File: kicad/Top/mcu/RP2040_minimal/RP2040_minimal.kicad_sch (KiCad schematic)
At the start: 39 parts, among them J2 Conn_01x02, U2 W25Q128JVS, U3 RP2040, Y1 ABLS-12.000MHZ-B4-T

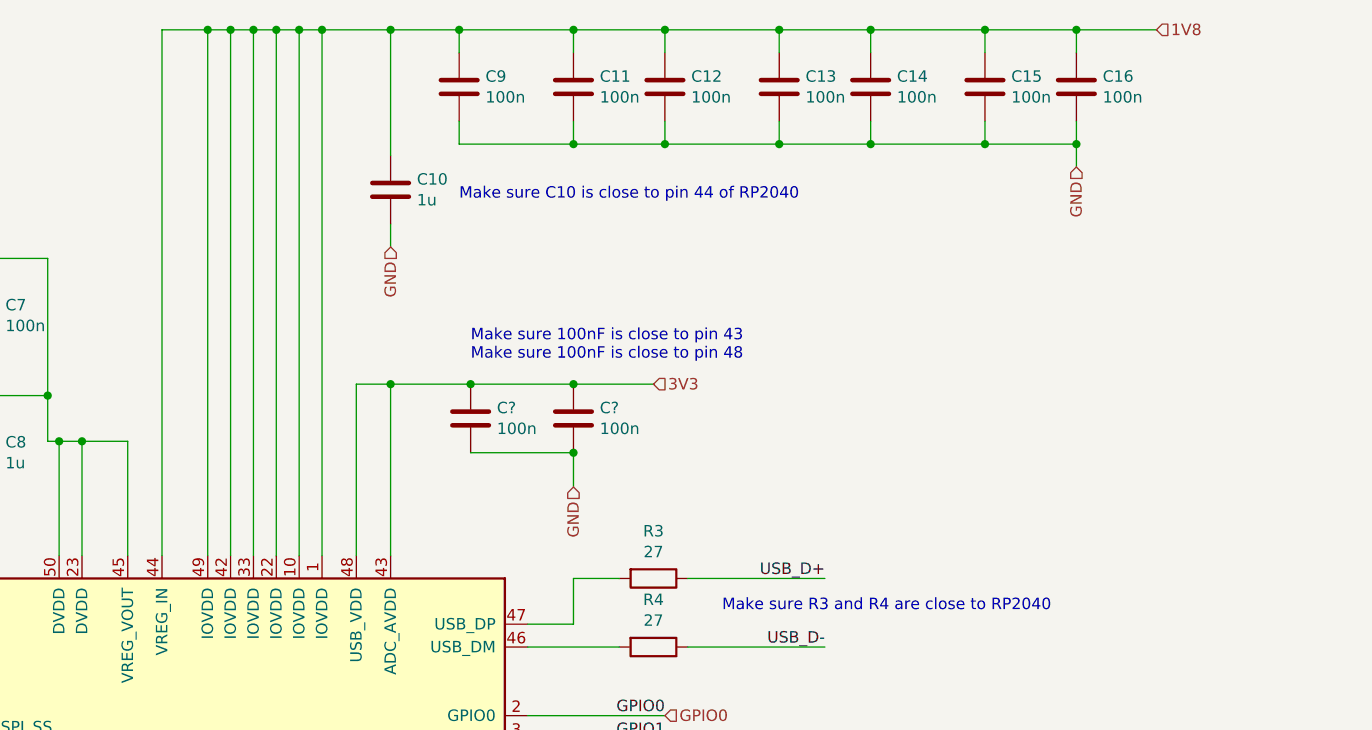
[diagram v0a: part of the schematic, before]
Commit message: Revert "Seperated and added 3V3 to MCU for USB and AVD supply"
This reverts commit dff833df8ca7cc74c4733d65dcaa8f38f7d04b29.
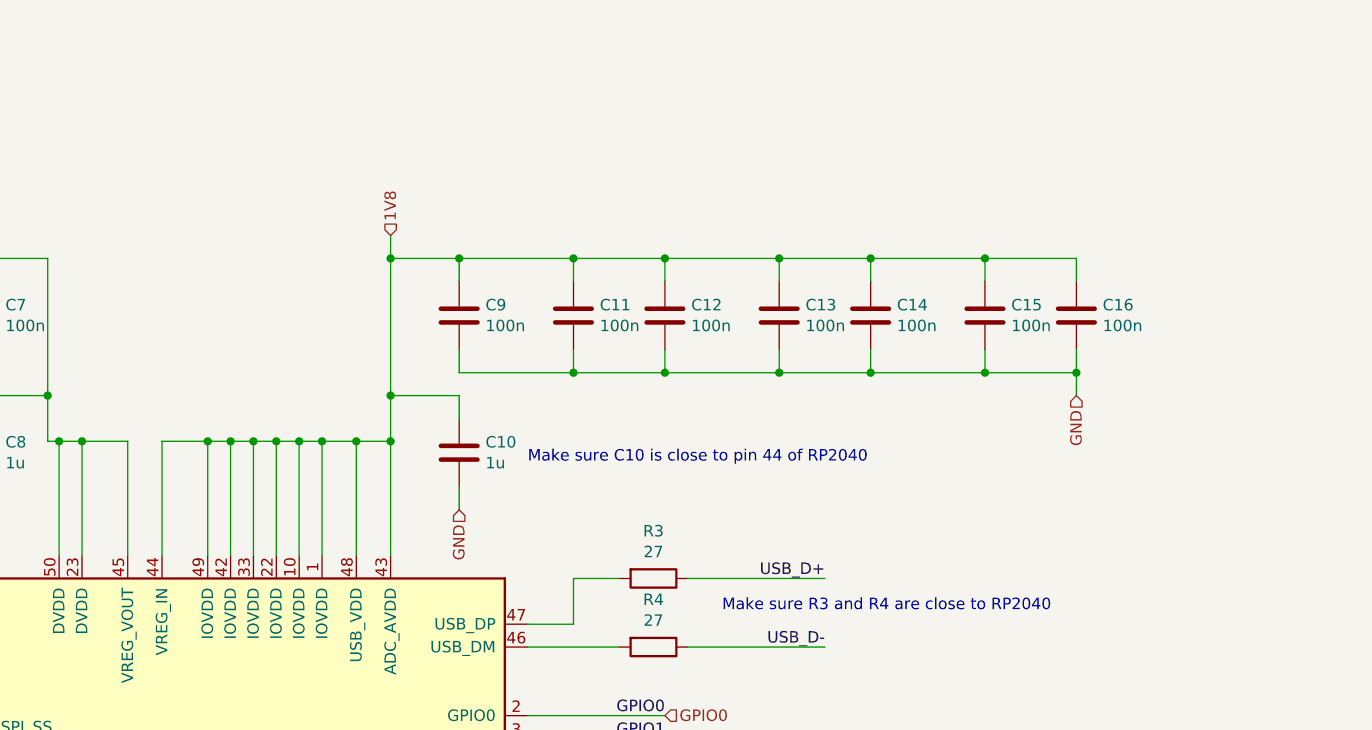
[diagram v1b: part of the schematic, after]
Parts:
- removed C? (x2): 100n, Capacitor_SMD:C_0402_1005Metric, symbol Device:C
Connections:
- net 1V8: now also U3.43 (ADC_AVDD), U3.48 (USB_VDD)
- net 3V3: no longer U3.43 (ADC_AVDD), U3.48 (USB_VDD)
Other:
- note removed: "Make sure 100nF is close to pin 43 Make sure 100nF is close to pin 48"
- moved on the sheet: C10, C11, C12, C13, C14, C15, C16, C9

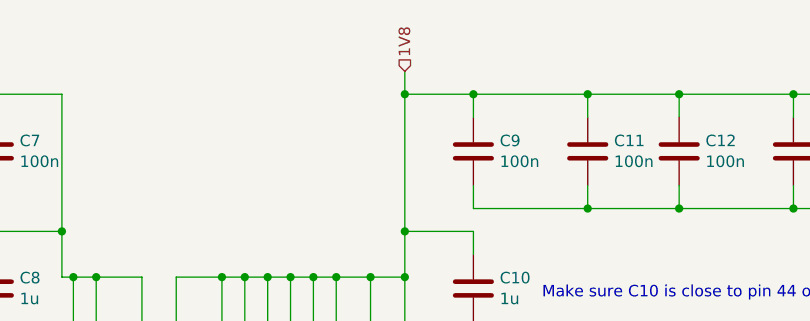
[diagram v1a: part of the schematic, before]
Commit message: Changed VIO to 3V3
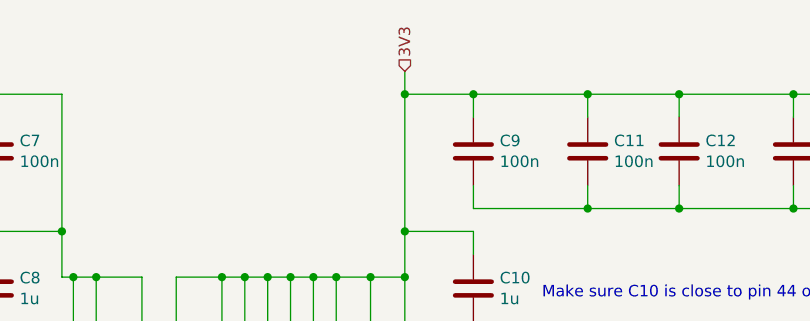
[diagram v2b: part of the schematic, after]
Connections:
- net 1V8: no longer C10.1, C11.1, C12.1, C13.1, C14.1, C15.1, C16.1, C9.1, U3.1 (IOVDD), U3.10 (IOVDD), U3.22 (IOVDD), U3.33 (IOVDD), U3.42 (IOVDD), U3.43 (ADC_AVDD), U3.44 (VREG_IN), U3.48 (USB_VDD), U3.49 (IOVDD)
- net 3V3: now also C10.1, C11.1, C12.1, C13.1, C14.1, C15.1, C16.1, C9.1, U3.1 (IOVDD), U3.10 (IOVDD), U3.22 (IOVDD), U3.33 (IOVDD), U3.42 (IOVDD), U3.43 (ADC_AVDD), U3.44 (VREG_IN), U3.48 (USB_VDD), U3.49 (IOVDD)
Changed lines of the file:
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@@
     (effects (font (size 1.27 1.27)) (justify left))
   )
-  (hierarchical_label "1V8" (shape input) (at 215.9 58.42 90)
+  (hierarchical_label "3V3" (shape input) (at 215.9 58.42 90)
     (effects (font (size 1.27 1.27)) (justify left))
   )
